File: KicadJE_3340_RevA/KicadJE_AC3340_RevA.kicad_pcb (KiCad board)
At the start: 2 copper layers, 100 x 100 mm, 2 parts, among them SW301 SW_DPDT_x2

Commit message: rev a
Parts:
- removed H401: 2,2mm, MountingHole:MountingHole_2.2mm_M2_Pad_Via
- removed SW301: SW_DPDT_x2, AJ:Johansen_engineering_logo_20mm
- added C101: 100n, Capacitor_SMD:C_0805_2012Metric_Pad1.15x1.40mm_HandSolder, B.Cu at (210.1, 81.4)
- added C102: 1n, Capacitor_SMD:C_0805_2012Metric_Pad1.15x1.40mm_HandSolder, B.Cu at (224.1, 100.3)
- added C103: 1n, Capacitor_SMD:C_0805_2012Metric_Pad1.15x1.40mm_HandSolder, B.Cu at (199.6, 75.1)
- added C104: 10n, Capacitor_SMD:C_0805_2012Metric_Pad1.15x1.40mm_HandSolder, B.Cu at (235.5, 111.2)
- added C105: 10n, Capacitor_SMD:C_0805_2012Metric_Pad1.15x1.40mm_HandSolder, B.Cu at (228.9, 100.3)
- added C106: 10n, Capacitor_SMD:C_0805_2012Metric_Pad1.15x1.40mm_HandSolder, B.Cu at (224.2, 94.4)
- added C107: 220p, Capacitor_SMD:C_0805_2012Metric_Pad1.15x1.40mm_HandSolder, B.Cu at (201.6, 72.2)
- added C108: 100n, Capacitor_SMD:C_0805_2012Metric_Pad1.15x1.40mm_HandSolder, B.Cu at (233.8, 105.3)
- added C109: 100n, Capacitor_SMD:C_0805_2012Metric_Pad1.15x1.40mm_HandSolder, B.Cu at (224.1, 103.3)
- added C110: 1n poly, Capacitor_THT:C_Rect_L7.0mm_W2.0mm_P5.00mm, B.Cu at (223.2, 113.2)
- added C111: 1n alt, Capacitor_SMD:C_0805_2012Metric_Pad1.15x1.40mm_HandSolder, B.Cu at (192.1, 66.2)
- added C112: 1u, Capacitor_SMD:C_1206_3216Metric_Pad1.42x1.75mm_HandSolder, B.Cu at (181.0, 65.8)
- added C113: 1u, Capacitor_SMD:C_1206_3216Metric_Pad1.42x1.75mm_HandSolder, B.Cu at (224.4, 109.8)
- added C114: 100n, Capacitor_SMD:C_0805_2012Metric_Pad1.15x1.40mm_HandSolder, B.Cu at (213.7, 90.5)
- added C115: 100n, Capacitor_SMD:C_0805_2012Metric_Pad1.15x1.40mm_HandSolder, B.Cu at (229.1, 106.6)
- added C116: 100n, Capacitor_SMD:C_0805_2012Metric_Pad1.15x1.40mm_HandSolder, B.Cu at (205.4, 81.4)
- added C117: 100n, Capacitor_SMD:C_0805_2012Metric_Pad1.15x1.40mm_HandSolder, B.Cu at (211.1, 84.6)
- added C118: 100n, Capacitor_SMD:C_0805_2012Metric_Pad1.15x1.40mm_HandSolder, B.Cu at (199.6, 78.1)
- added C119: 100n, Capacitor_SMD:C_0805_2012Metric_Pad1.15x1.40mm_HandSolder, B.Cu at (191.1, 69.1)
- added D101: 1N1007, Diode_SMD:D_SOD-123, B.Cu at (223.8, 106.4)
- added D102: 1N1007, Diode_SMD:D_SOD-123, B.Cu at (200.1, 84.6)
- added D103: 1N1007, Diode_SMD:D_SOD-123, B.Cu at (200.1, 81.2)
- added D104: 1N1007, Diode_SMD:D_SOD-123, B.Cu at (213.1, 100.4)
- added D105: 1N1007, Diode_SMD:D_SOD-123, B.Cu at (191.6, 72.3)
- added D106: 1N1007, Diode_SMD:D_SOD-123, B.Cu at (186.9, 65.7)
- added D107: 1N1007, Diode_SMD:D_SOD-123, B.Cu at (230.2, 109.7)
- added D108: 1N1007, Diode_SMD:D_SOD-123, B.Cu at (240.7, 121.0)
- added D109: 1N1007, Diode_SMD:D_SOD-123, B.Cu at (235.0, 114.3)
- added D110: 1N1007, Diode_SMD:D_SOD-123, B.Cu at (205.9, 84.6)
- added D111: 1N1007, Diode_SMD:D_SOD-123, B.Cu at (218.9, 97.0)
- added D112: 1N4148, Diode_SMD:D_SOD-123, B.Cu at (214.2, 93.7)
- added D113: 1N1007, Diode_SMD:D_SOD-123, B.Cu at (218.9, 100.4)
- added D114: 1N1007, Diode_SMD:D_SOD-123, B.Cu at (213.1, 97.0)
- added D115: Germanium, Diode_THT:D_A-405_P7.62mm_Horizontal, F.Cu at (65.0, 157.0)
- added D116: LED, LED_SMD:LED_0805_2012Metric_Pad1.15x1.40mm_HandSolder, F.Cu at (70.0, 75.0)
- added D117: 1N1007, Diode_SMD:D_SOD-123, B.Cu at (235.0, 121.0)
- added D118: 1N1007, Diode_SMD:D_SOD-123, B.Cu at (235.0, 117.7)
- added J101: RampOut1, AJ-Dropbox-Kicad:PJ301SM, F.Cu at (80.0, 125.0)
- added J102: PulseOut2, AJ-Dropbox-Kicad:PJ301SM, F.Cu at (80.0, 115.0)
- added J103: SawOut3, AJ-Dropbox-Kicad:PJ301SM, F.Cu at (80.0, 145.0)
- added J104: In1.1, AJ-Dropbox-Kicad:PJ301SM, F.Cu at (60.0, 85.0)
- added J105: In1.2, AJ-Dropbox-Kicad:PJ301SM, F.Cu at (60.0, 95.0)
- added J106: In1.3, AJ-Dropbox-Kicad:PJ301SM, F.Cu at (60.0, 105.0)
- added J107: SS_In2, AJ-Dropbox-Kicad:PJ301SM, F.Cu at (60.0, 135.0)
- added J108: HS_In3, AJ-Dropbox-Kicad:PJ301SM, F.Cu at (60.0, 145.0)
- added J109: FM_In4, AJ-Dropbox-Kicad:PJ301SM, F.Cu at (60.0, 115.0)
- added J110: PWM_In5, AJ-Dropbox-Kicad:PJ301SM, F.Cu at (60.0, 125.0)
- added J111: SineOut4, AJ-Dropbox-Kicad:PJ301SM, F.Cu at (80.0, 135.0)
- added JP101: Jumper_3_Bridged12, Jumper:SolderJumper-3_P1.3mm_Bridged12_Pad1.0x1.5mm_NumberLabels, B.Cu at (240.7, 117.6)
- added P101: HEADER_2x5_Doepfer, Connector_IDC:IDC-Header_2x05_P2.54mm_Vertical, B.Cu at (75.0, 56.0)
- added Q101: MMBT3906, Package_TO_SOT_SMD:SOT-23, B.Cu at (247.9, 105.3)
- added Q102: UMX1N, AJ:UMX1N_UMT6_DualNPN, B.Cu at (235.2, 76.4)
- added R101: 47k, Resistor_SMD:R_0805_2012Metric_Pad1.15x1.40mm_HandSolder, B.Cu at (218.5, 90.5)
- added R102: 470R, Resistor_SMD:R_0805_2012Metric_Pad1.15x1.40mm_HandSolder, B.Cu at (196.9, 72.2)
- added R103: 82k, Resistor_SMD:R_0805_2012Metric_Pad1.15x1.40mm_HandSolder, B.Cu at (235.5, 108.2)
- added R104: 20k, Resistor_SMD:R_0805_2012Metric_Pad1.15x1.40mm_HandSolder, B.Cu at (245.9, 117.9)
- added R105: 1k, Resistor_SMD:R_0805_2012Metric_Pad1.15x1.40mm_HandSolder, B.Cu at (219.5, 93.9)
- added R106: 910R, Resistor_SMD:R_0805_2012Metric_Pad1.15x1.40mm_HandSolder, B.Cu at (240.2, 114.3)
- added R107: 1k, Resistor_SMD:R_0805_2012Metric_Pad1.15x1.40mm_HandSolder, B.Cu at (204.4, 78.1)
- added R108: 100k, Resistor_SMD:R_0805_2012Metric_Pad1.15x1.40mm_HandSolder, B.Cu at (213.7, 87.6)
- added R109: 100k, Resistor_SMD:R_0805_2012Metric_Pad1.15x1.40mm_HandSolder, B.Cu at (224.1, 97.4)
- added R110: 100k, Resistor_SMD:R_0805_2012Metric_Pad1.15x1.40mm_HandSolder, B.Cu at (246.0, 121.2)
- added R111: 1k, Resistor_SMD:R_0805_2012Metric_Pad1.15x1.40mm_HandSolder, B.Cu at (240.2, 111.4)
- added R112: 1k, Resistor_SMD:R_0805_2012Metric_Pad1.15x1.40mm_HandSolder, B.Cu at (228.9, 103.3)
- added R113: 1k, Resistor_SMD:R_0805_2012Metric_Pad1.15x1.40mm_HandSolder, B.Cu at (243.1, 99.6)
- added R114: 1k6, Resistor_SMD:R_0805_2012Metric_Pad1.15x1.40mm_HandSolder, B.Cu at (218.6, 75.8)
- added R115: 1M, Resistor_SMD:R_0805_2012Metric_Pad1.15x1.40mm_HandSolder, B.Cu at (238.5, 93.5)
- added R116: 1k, Resistor_SMD:R_0805_2012Metric_Pad1.15x1.40mm_HandSolder, B.Cu at (211.1, 66.3)
- added R117: 360k, Resistor_SMD:R_0805_2012Metric_Pad1.15x1.40mm_HandSolder, B.Cu at (224.4, 78.7)
- added R118: 470R, Resistor_SMD:R_0805_2012Metric_Pad1.15x1.40mm_HandSolder, B.Cu at (232.7, 87.6)
- added R119: 1M, Resistor_SMD:R_0805_2012Metric_Pad1.15x1.40mm_HandSolder, B.Cu at (214.9, 69.6)
- added R120: 100k, Resistor_SMD:R_0805_2012Metric_Pad1.15x1.40mm_HandSolder, B.Cu at (224.4, 81.7)
- added R121: 12k5, Resistor_SMD:R_0805_2012Metric_Pad1.15x1.40mm_HandSolder, B.Cu at (238.6, 105.3)
- added R122: 100k, Resistor_SMD:R_0805_2012Metric_Pad1.15x1.40mm_HandSolder, B.Cu at (228.9, 97.4)
- added R123: 100k, Resistor_SMD:R_0805_2012Metric_Pad1.15x1.40mm_HandSolder, B.Cu at (215.9, 84.6)
- added R124: 100k, Resistor_SMD:R_0805_2012Metric_Pad1.15x1.40mm_HandSolder, B.Cu at (218.5, 87.6)
- added R125: 470R, Resistor_SMD:R_0805_2012Metric_Pad1.15x1.40mm_HandSolder, B.Cu at (245.9, 114.9)
- added R126: 10k, Resistor_SMD:R_0805_2012Metric_Pad1.15x1.40mm_HandSolder, B.Cu at (196.9, 66.2)
- added R127: 10k, Resistor_SMD:R_0805_2012Metric_Pad1.15x1.40mm_HandSolder, B.Cu at (209.1, 78.5)
- added R128: 12k5, Resistor_SMD:R_0805_2012Metric_Pad1.15x1.40mm_HandSolder, B.Cu at (200.6, 69.2)
- added R129: 1M5, Resistor_SMD:R_0805_2012Metric_Pad1.15x1.40mm_HandSolder, B.Cu at (245.0, 112.0)
- added R130: 10k, Resistor_SMD:R_0805_2012Metric_Pad1.15x1.40mm_HandSolder, B.Cu at (220.6, 84.6)
- added R131: 10k, Resistor_SMD:R_0805_2012Metric_Pad1.15x1.40mm_HandSolder, B.Cu at (201.6, 66.3)
- added R132: 100k, Resistor_SMD:R_0805_2012Metric_Pad1.15x1.40mm_HandSolder, B.Cu at (205.4, 69.2)
- added R133: 100k, Resistor_SMD:R_0805_2012Metric_Pad1.15x1.40mm_HandSolder, B.Cu at (238.4, 102.3)
- added R134: 10k, Resistor_SMD:R_0805_2012Metric_Pad1.15x1.40mm_HandSolder, B.Cu at (223.2, 88.0)
- added R135: 47k, Resistor_SMD:R_0805_2012Metric_Pad1.15x1.40mm_HandSolder, B.Cu at (214.9, 78.7)
- added R136: 47k, Resistor_SMD:R_0805_2012Metric_Pad1.15x1.40mm_HandSolder, B.Cu at (245.0, 109.0)
- added R137: 47k, Resistor_SMD:R_0805_2012Metric_Pad1.15x1.40mm_HandSolder, B.Cu at (206.4, 72.2)
- added R138: 22k, Resistor_SMD:R_0805_2012Metric_Pad1.15x1.40mm_HandSolder, B.Cu at (219.6, 81.7)
- added R139: 2k20, Resistor_SMD:R_0805_2012Metric_Pad1.15x1.40mm_HandSolder, B.Cu at (209.1, 75.5)
- added R140: 10k, Resistor_SMD:R_0805_2012Metric_Pad1.15x1.40mm_HandSolder, B.Cu at (233.6, 99.4)
- added R141: 390R, Resistor_SMD:R_0805_2012Metric_Pad1.15x1.40mm_HandSolder, B.Cu at (229.0, 94.4)
- added R142: 18k, Resistor_SMD:R_0805_2012Metric_Pad1.15x1.40mm_HandSolder, B.Cu at (204.4, 75.1)
- added R143: 10k, Resistor_SMD:R_0805_2012Metric_Pad1.15x1.40mm_HandSolder, B.Cu at (214.9, 81.7)
- added R144: 26k7, Resistor_SMD:R_0805_2012Metric_Pad1.15x1.40mm_HandSolder, B.Cu at (223.2, 90.9)
- added R145: 6k04, Resistor_SMD:R_0805_2012Metric_Pad1.15x1.40mm_HandSolder, B.Cu at (233.6, 102.3)
- added R146: 1M2, Resistor_SMD:R_0805_2012Metric_Pad1.15x1.40mm_HandSolder, B.Cu at (240.2, 108.4)
- added R147: 2k20, Resistor_SMD:R_0805_2012Metric_Pad1.15x1.40mm_HandSolder, B.Cu at (195.9, 69.1)
- added R148: 1k82, Resistor_SMD:R_0805_2012Metric_Pad1.15x1.40mm_HandSolder, B.Cu at (243.3, 105.5)
- added R149: 13k3, Resistor_SMD:R_0805_2012Metric_Pad1.15x1.40mm_HandSolder, B.Cu at (233.7, 96.4)
- added R150: 13k3, Resistor_SMD:R_0805_2012Metric_Pad1.15x1.40mm_HandSolder, B.Cu at (238.4, 99.4)
- added R151: OPEN, Resistor_SMD:R_0805_2012Metric_Pad1.15x1.40mm_HandSolder, B.Cu at (213.9, 75.8)
- added R152: 0R, Resistor_SMD:R_0805_2012Metric_Pad1.15x1.40mm_HandSolder, B.Cu at (211.1, 72.6)
- added R153: 1k, Resistor_SMD:R_0805_2012Metric_Pad1.15x1.40mm_HandSolder, B.Cu at (233.7, 93.5)
- added R154: 3k, Resistor_SMD:R_0805_2012Metric_Pad1.15x1.40mm_HandSolder, B.Cu at (228.0, 88.5)
- added R155: 1k, Resistor_SMD:R_0805_2012Metric_Pad1.15x1.40mm_HandSolder, B.Cu at (206.4, 66.3)
- added R156: 100k, Resistor_SMD:R_0805_2012Metric_Pad1.15x1.40mm_HandSolder, B.Cu at (219.6, 78.7)
- added R157: 15k, Resistor_SMD:R_0805_2012Metric_Pad1.15x1.40mm_HandSolder, B.Cu at (243.3, 102.5)
- added R158: 10k, Resistor_SMD:R_0805_2012Metric_Pad1.15x1.40mm_HandSolder, B.Cu at (225.4, 85.0)
- added R159: 10k, Resistor_SMD:R_0805_2012Metric_Pad1.15x1.40mm_HandSolder, B.Cu at (210.1, 69.2)
- added R160: 25k, Resistor_SMD:R_0805_2012Metric_Pad1.15x1.40mm_HandSolder, B.Cu at (228.0, 91.5)
- added R161: 10k, Resistor_SMD:R_0805_2012Metric_Pad1.15x1.40mm_HandSolder, B.Cu at (238.5, 96.4)
- added R162: 25k, Resistor_SMD:R_0805_2012Metric_Pad1.15x1.40mm_HandSolder, B.Cu at (215.9, 72.8)
- added R163: OPEN, Resistor_SMD:R_0805_2012Metric_Pad1.15x1.40mm_HandSolder, B.Cu at (232.7, 90.5)
- added RV101: 100k Fine, AJ-Dropbox-Kicad:Potentiometer_China_RK09_Single_Vertical_AJ, F.Cu at (72.0, 68.0)
- added RV102: 100k PWM, AJ-Dropbox-Kicad:Potentiometer_China_RK09_Single_Vertical_AJ, F.Cu at (67.0, 63.0)
- added RV103: 5k, Potentiometer_THT:Potentiometer_Bourns_3296W_Vertical, B.Cu at (218.4, 119.5)
- added RV104: 50k, Potentiometer_THT:Potentiometer_Bourns_3296W_Vertical, B.Cu at (218.4, 113.0)
- added SW101: Octave (3 state), AJ-Dropbox-Kicad:SP1MS1, F.Cu at (80.0, 85.0)
- added U101: TL072, AJ-Dropbox-Kicad:AJ_SO-8_5.3x6.2mm_P1.27mm, B.Cu at (195.3, 90.1)
- added U102: TL072, AJ-Dropbox-Kicad:AJ_SO-8_5.3x6.2mm_P1.27mm, B.Cu at (185.2, 79.0)
- added U103: TL072, AJ-Dropbox-Kicad:AJ_SO-8_5.3x6.2mm_P1.27mm, B.Cu at (183.4, 71.3)
- added U104: AS3340, Package_DIP:DIP-16_W10.16mm_LongPads, B.Cu at (85.0, 92.0)
- added U105: L78L05_SOT89, Package_TO_SOT_SMD:SOT-89-3, B.Cu at (193.5, 83.2)
- added U106: L79L05_SOT89, Package_TO_SOT_SMD:SOT-89-3, B.Cu at (193.5, 77.0)
- added U107: TL072, AJ-Dropbox-Kicad:AJ_SO-8_5.3x6.2mm_P1.27mm, B.Cu at (226.8, 118.8)

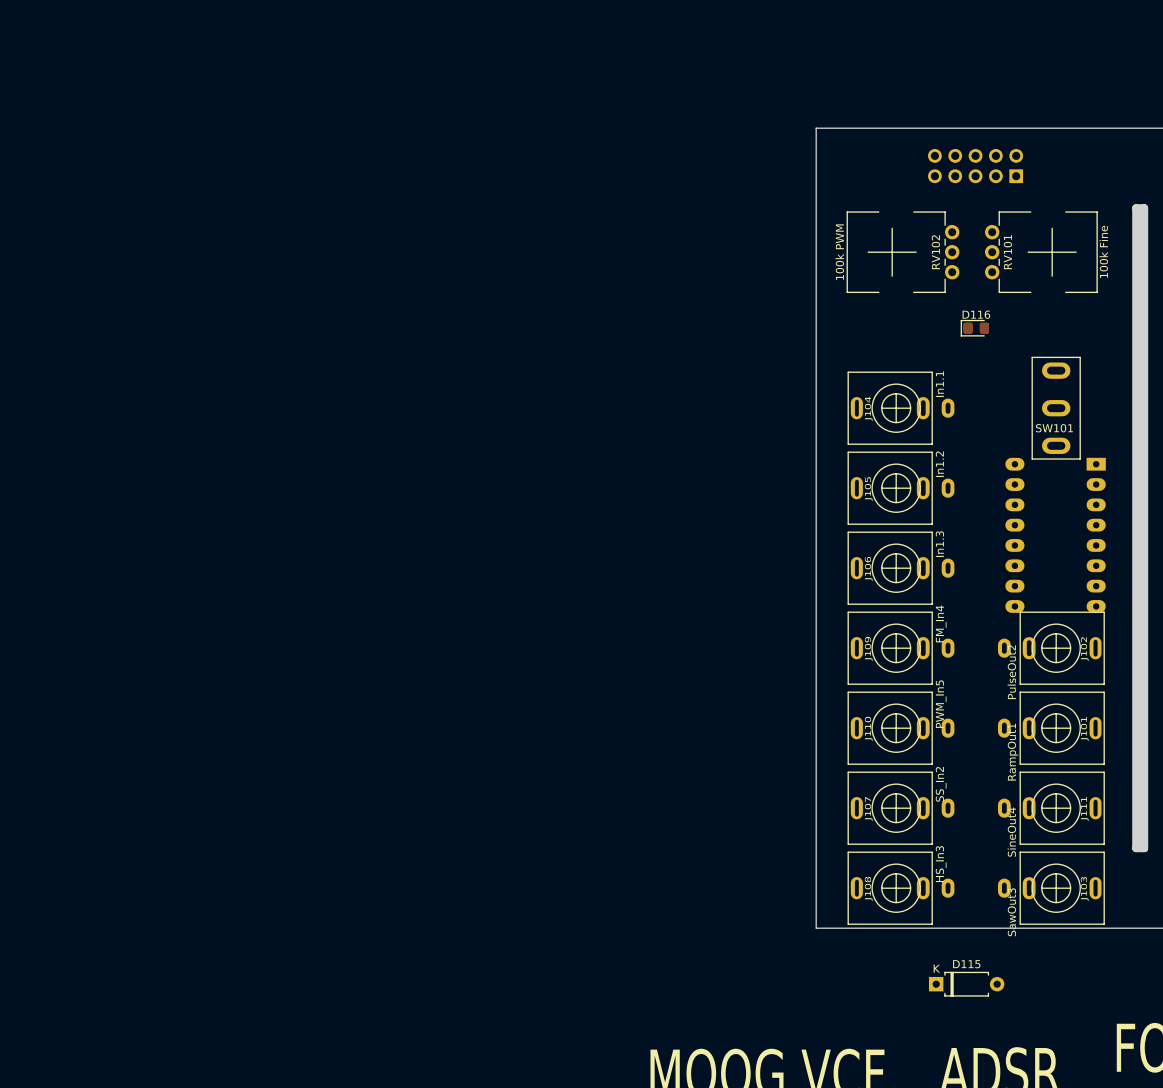
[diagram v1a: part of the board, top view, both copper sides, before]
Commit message: Update KicadJE_AC3340_RevA.kicad_pcb
Front Panel Guides
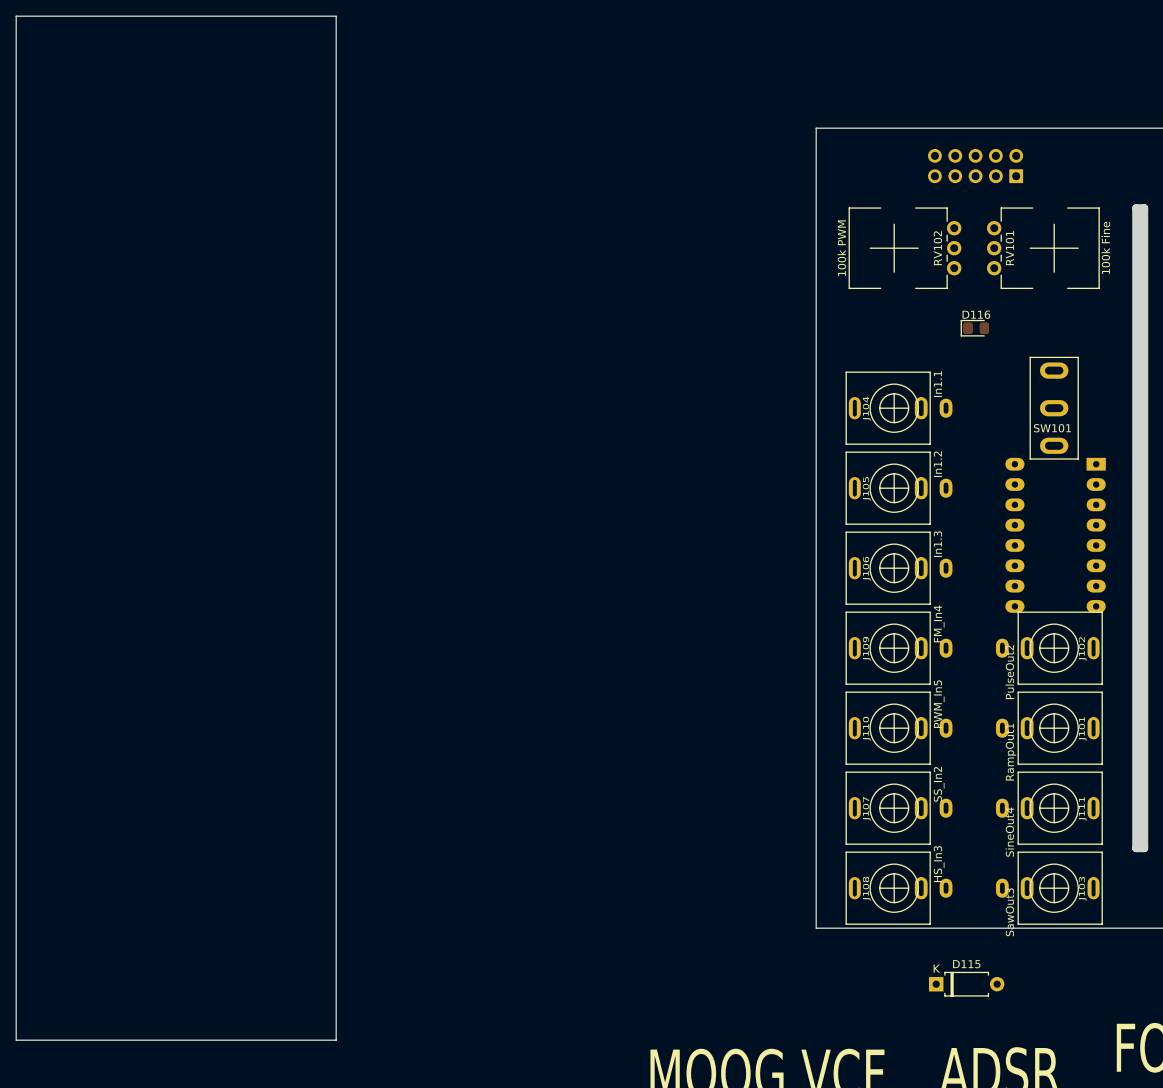
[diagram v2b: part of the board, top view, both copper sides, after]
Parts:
- moved RV101 0.56 mm to (72.2, 67.5)
- moved RV102 0.56 mm to (67.2, 62.5)
- moved J101 0.25 mm to (79.8, 125.0)
- moved J102 0.25 mm to (79.8, 115.0)
- moved J103 0.25 mm to (79.8, 145.0)
- moved J104 0.25 mm to (59.8, 85.0)
- moved J105 0.25 mm to (59.8, 95.0)
- moved J106 0.25 mm to (59.8, 105.0)
- moved J107 0.25 mm to (59.8, 135.0)
- moved J108 0.25 mm to (59.8, 145.0)
- moved J109 0.25 mm to (59.8, 115.0)
- moved J110 0.25 mm to (59.8, 125.0)
- moved J111 0.25 mm to (79.8, 135.0)
- moved SW101 0.25 mm to (79.8, 85.0)
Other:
- board size 100 x 100 mm -> 200 x 128 mm
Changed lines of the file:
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@@
   (general
     (thickness 1.6)
-    (drawings 44)
+    (drawings 83)
     (tracks 0)
     (zones 0)
@@
   )
   (module AJ-Dropbox-Kicad:PJ301SM (layer F.Cu)
-    (at 80 125 270)
+    (at 79.75 125 270)
     (fp_text reference J101 (at 0 -3.5 270) (layer F.SilkS)
       (effects (font (size 0.75 1) (thickness 0.125)))
@@
   )
   (module AJ-Dropbox-Kicad:PJ301SM (layer F.Cu)
-    (at 80 115 270)
+    (at 79.75 115 270)
     (fp_text reference J102 (at 0 -3.5 270) (layer F.SilkS)
       (effects (font (size 0.75 1) (thickness 0.125)))
@@
   )
   (module AJ-Dropbox-Kicad:PJ301SM (layer F.Cu)
-    (at 80 145 270)
+    (at 79.75 145 270)
     (fp_text reference J103 (at 0 -3.5 270) (layer F.SilkS)
       (effects (font (size 0.75 1) (thickness 0.125)))
@@
   )
   (module AJ-Dropbox-Kicad:PJ301SM (layer F.Cu)
-    (at 60 85 90)
+    (at 59.75 85 90)
     (fp_text reference J104 (at 0 -3.5 90) (layer F.SilkS)
       (effects (font (size 0.75 1) (thickness 0.125)))
@@
   )
   (module AJ-Dropbox-Kicad:PJ301SM (layer F.Cu)
-    (at 60 95 90)
+    (at 59.75 95 90)
     (fp_text reference J105 (at 0 -3.5 90) (layer F.SilkS)
       (effects (font (size 0.75 1) (thickness 0.125)))
@@
   )
   (module AJ-Dropbox-Kicad:PJ301SM (layer F.Cu)
-    (at 60 105 90)
+    (at 59.75 105 90)
     (fp_text reference J106 (at 0 -3.5 90) (layer F.SilkS)
       (effects (font (size 0.75 1) (thickness 0.125)))
@@
   )
   (module AJ-Dropbox-Kicad:PJ301SM (layer F.Cu)
-    (at 60 135 90)
+    (at 59.75 135 90)
     (fp_text reference J107 (at 0 -3.5 90) (layer F.SilkS)
       (effects (font (size 0.75 1) (thickness 0.125)))
@@
   )
   (module AJ-Dropbox-Kicad:PJ301SM (layer F.Cu)
-    (at 60 145 90)
+    (at 59.75 145 90)
     (fp_text reference J108 (at 0 -3.5 90) (layer F.SilkS)
       (effects (font (size 0.75 1) (thickness 0.125)))
@@
   )
   (module AJ-Dropbox-Kicad:PJ301SM (layer F.Cu)
-    (at 60 115 90)
+    (at 59.75 115 90)
     (fp_text reference J109 (at 0 -3.5 90) (layer F.SilkS)
       (effects (font (size 0.75 1) (thickness 0.125)))
@@
   )
   (module AJ-Dropbox-Kicad:PJ301SM (layer F.Cu)
-    (at 60 125 90)
+    (at 59.75 125 90)
     (fp_text reference J110 (at 0 -3.5 90) (layer F.SilkS)
       (effects (font (size 0.75 1) (thickness 0.125)))
@@
   )
   (module AJ-Dropbox-Kicad:PJ301SM (layer F.Cu)
-    (at 80 135 270)
+    (at 79.75 135 270)
     (fp_text reference J111 (at 0 -3.5 270) (layer F.SilkS)
       (effects (font (size 0.75 1) (thickness 0.125)))
@@
   )
   (module AJ-Dropbox-Kicad:Potentiometer_China_RK09_Single_Vertical_AJ (layer F.Cu)
-    (at 72 68)
+    (at 72.25 67.5)
     (descr "Potentiometer, vertical, Alps RK09K Single, http://www.alps.com/prod/info/E/HTML/Potentiometer/RotaryPotentiometers/RK09K/RK09K_list.html")
     (tags "Potentiometer vertical Alps RK09K Single")
@@
   )
   (module AJ-Dropbox-Kicad:Potentiometer_China_RK09_Single_Vertical_AJ (layer F.Cu)
-    (at 67 63 180)
+    (at 67.25 62.5 180)
     (descr "Potentiometer, vertical, Alps RK09K Single, http://www.alps.com/prod/info/E/HTML/Potentiometer/RotaryPotentiometers/RK09K/RK09K_list.html")
     (tags "Potentiometer vertical Alps RK09K Single")
@@
   )
   (module AJ-Dropbox-Kicad:SP1MS1 (layer F.Cu)
-    (at 80 85)
+    (at 79.75 85)
     (fp_text reference SW101 (at -0.2 2.54) (layer F.SilkS)
       (effects (font (size 1 1) (thickness 0.15)))
@@
     )
   )
+  (gr_line (start -16.5 36) (end -16.5 164) (layer Dwgs.User) (width 0.15))
+  (gr_line (start -43.5 36) (end -43.5 164) (layer Dwgs.User) (width 0.15))
+  (gr_line (start -50 160.5) (end -10 160.5) (layer Dwgs.User) (width 0.15))
+  (gr_line (start -50 38.5) (end -10 38.5) (layer Dwgs.User) (width 0.15))
+  (gr_line (start -50 164) (end -50 36) (layer Edge.Cuts) (width 0.05))
+  (gr_line (start -10 164) (end -50 164) (layer Edge.Cuts) (width 0.05))
+  (gr_line (start -10 36) (end -10 164) (layer Edge.Cuts) (width 0.05))
+  (gr_line (start -50 36) (end -10 36) (layer Edge.Cuts) (width 0.05))
+  (gr_circle (center -40 145) (end -43.25 145.5) (layer Dwgs.User) (width 0.15))
+  (gr_circle (center -20 115) (end -23.25 115.5) (layer Dwgs.User) (width 0.15))
+  (gr_circle (center -40 95) (end -43.25 95.5) (layer Dwgs.User) (width 0.15))
+  (gr_circle (center -40 125) (end -43.25 125.5) (layer Dwgs.User) (width 0.15))
+  (gr_circle (center -40 85) (end -43.25 85.5) (layer Dwgs.User) (width 0.15))
+  (gr_circle (center -20 145) (end -23.25 145.5) (layer Dwgs.User) (width 0.15))
+  (gr_circle (center -20 135) (end -23.25 135.5) (layer Dwgs.User) (width 0.15))
+  (gr_circle (center -40 105) (end -43.25 105.5) (layer Dwgs.User) (width 0.15))
+  (gr_circle (center -20 65) (end -23.25 65.5) (layer Dwgs.User) (width 0.15))
+  (gr_circle (center -20 85) (end -23.25 85.5) (layer Dwgs.User) (width 0.15))
+  (gr_circle (center -40 65) (end -43.25 65.5) (layer Dwgs.User) (width 0.15))
+  (gr_circle (center -40 135) (end -43.25 135.5) (layer Dwgs.User) (width 0.15))
+  (gr_circle (center -20 125) (end -23.25 125.5) (layer Dwgs.User) (width 0.15))
+  (gr_circle (center -40 115) (end -43.25 115.5) (layer Dwgs.User) (width 0.15))
+  (gr_line (start -20 50) (end -20 150) (layer Dwgs.User) (width 0.15))
+  (gr_line (start -30 50) (end -30 150) (layer Dwgs.User) (width 0.15))
+  (gr_line (start -40 150) (end -40 50) (layer Dwgs.User) (width 0.15))
+  (gr_circle (center 59.75 85) (end 56.5 85.5) (layer Dwgs.User) (width 0.15))
+  (gr_circle (center 79.75 125) (end 76.5 125.5) (layer Dwgs.User) (width 0.15))
+  (gr_circle (center 79.75 115) (end 76.5 115.5) (layer Dwgs.User) (width 0.15))
+  (gr_circle (center 79.75 85) (end 76.5 85.5) (layer Dwgs.User) (width 0.15))
+  (gr_circle (center 79.75 135) (end 76.5 135.5) (layer Dwgs.User) (width 0.15))
+  (gr_circle (center 79.75 145) (end 76.5 145.5) (layer Dwgs.User) (width 0.15))
+  (gr_circle (center 59.75 145) (end 56.5 145.5) (layer Dwgs.User) (width 0.15))
+  (gr_circle (center 59.75 135) (end 56.5 135.5) (layer Dwgs.User) (width 0.15))
+  (gr_circle (center 59.75 125) (end 56.5 125.5) (layer Dwgs.User) (width 0.15))
+  (gr_circle (center 59.75 115) (end 56.5 115.5) (layer Dwgs.User) (width 0.15))
+  (gr_circle (center 59.75 105) (end 56.5 105.5) (layer Dwgs.User) (width 0.15))
+  (gr_circle (center 59.75 95) (end 56.5 95.5) (layer Dwgs.User) (width 0.15))
+  (gr_circle (center 79.75 65) (end 76.5 65.5) (layer Dwgs.User) (width 0.15))
+  (gr_circle (center 59.75 65) (end 56.5 65.5) (layer Dwgs.User) (width 0.15))
   (gr_text "FOLDING\nWINDOW" (at 105.2 187.6) (layer B.SilkS)
     (effects (font (size 4 3) (thickness 0.75)) (justify mirror))
